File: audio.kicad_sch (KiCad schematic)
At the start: 6 parts, among them J6 AudioJack3, U8 LM386

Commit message: Updated Schematic
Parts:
- added C37: 250 uF, Capacitor_SMD:C_0805_2012Metric, symbol Device:C
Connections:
- net +5V: no longer C35.2
- net at C36.2, U8.5: now also C37.1; no longer J6.R, J6.T
- new net: C37.2, J6.R, J6.T
- new net AUDIO_IN: C35.2
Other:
- moved on the sheet: J6
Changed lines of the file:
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@@
 	(paper "A4")
 	(junction
-		(at 168.91 86.36)
+		(at 184.15 86.36)
 		(diameter 0)
 		(color 0 0 0 0)
@@
 	(wire
 		(pts
-			(xy 168.91 83.82) (xy 168.91 86.36)
+			(xy 184.15 83.82) (xy 184.15 86.36)
 		)
 		(stroke
@@
 	(wire
 		(pts
+			(xy 176.53 86.36) (xy 184.15 86.36)
+		)
+		(stroke
+			(width 0)
+			(type default)
+		)
+	)
+	(wire
+		(pts
 			(xy 135.89 88.9) (xy 130.81 88.9)
 		)
@@
 	(wire
 		(pts
-			(xy 171.45 88.9) (xy 171.45 93.98)
-		)
-		(stroke
-			(width 0)
-			(type default)
-		)
-	)
-	(wire
-		(pts
-			(xy 171.45 83.82) (xy 168.91 83.82)
+			(xy 186.69 88.9) (xy 186.69 93.98)
+		)
+		(stroke
+			(width 0)
+			(type default)
+		)
+	)
+	(wire
+		(pts
+			(xy 186.69 83.82) (xy 184.15 83.82)
+		)
+		(stroke
+			(width 0)
+			(type default)
+		)
+	)
+	(wire
+		(pts
+			(xy 199.39 123.19) (xy 231.14 123.19)
 		)
 		(stroke
@@
 	(wire
 		(pts
-			(xy 168.91 86.36) (xy 171.45 86.36)
+			(xy 184.15 86.36) (xy 186.69 86.36)
 		)
 		(stroke
@@
 		)
 	)
-	(symbol
-		(lib_id "power:+5V")
-		(at 123.19 64.77 0)
-		(unit 1)
-		(exclude_from_sim no)
-		(in_bom yes)
-		(on_board yes)
-		(dnp no)
-		(fields_autoplaced yes)
-		(property "Reference" "#PWR072"
-			(at 123.19 68.58 0)
-			(effects
-				(font
-					(size 1.27 1.27)
-				)
-				(hide yes)
-			)
-		)
-		(property "Value" "+5V"
-			(at 123.19 59.69 0)
-			(effects
-				(font
-					(size 1.27 1.27)
-				)
-			)
-		)
-		(property "Footprint" ""
-			(at 123.19 64.77 0)
-			(effects
-				(font
-					(size 1.27 1.27)
-				)
-				(hide yes)
-			)
-		)
-		(property "Datasheet" ""
-			(at 123.19 64.77 0)
-			(effects
-				(font
-					(size 1.27 1.27)
-				)
-				(hide yes)
-			)
-		)
-		(property "Description" "Power symbol creates a global label with name \"+5V\""
-			(at 123.19 64.77 0)
-			(effects
-				(font
-					(size 1.27 1.27)
-				)
-				(hide yes)
-			)
-		)
-		(pin "1"
-		)
-		(instances
-			(project ""
-				(path "/35c074f0-8545-4dc1-a57d-3ef0bc7d9188/b0fb54ab-b2e8-4f49-90f2-51362383cff9"
-					(reference "#PWR072")
-					(unit 1)
-				)
-			)
+	(global_label "AUDIO_OUT"
+		(shape input)
+		(at 199.39 123.19 180)
+		(fields_autoplaced yes)
+		(effects
+			(font
+				(size 1.27 1.27)
+			)
+			(justify right)
+		)
+		(property "Intersheetrefs" "${INTERSHEET_REFS}"
+			(at 186.1842 123.19 0)
+			(effects
+				(font
+					(size 1.27 1.27)
+				)
+				(justify right)
+				(hide yes)
+			)
+		)
+	)
+	(global_label "AUDIO_IN"
+		(shape input)
+		(at 123.19 64.77 90)
+		(fields_autoplaced yes)
+		(effects
+			(font
+				(size 1.27 1.27)
+			)
+			(justify left)
+		)
+		(property "Intersheetrefs" "${INTERSHEET_REFS}"
+			(at 123.19 53.2575 90)
+			(effects
+				(font
+					(size 1.27 1.27)
+				)
+				(justify left)
+				(hide yes)
+			)
+		)
+	)
+	(hierarchical_label "AUDIO_IN"
+		(shape input)
+		(at 231.14 123.19 0)
+		(effects
+			(font
+				(size 1.27 1.27)
+			)
+			(justify left)
 		)
 	)
@@
 	(symbol
 		(lib_id "power:GND")
-		(at 171.45 93.98 0)
+		(at 186.69 93.98 0)
 		(unit 1)
 		(exclude_from_sim no)
@@
 		(fields_autoplaced yes)
 		(property "Reference" "#PWR071"
-			(at 171.45 100.33 0)
+			(at 186.69 100.33 0)
 			(effects
 				(font
@@
 		)
 		(property "Value" "GND"
-			(at 171.45 99.06 0)
+			(at 186.69 99.06 0)
 			(effects
 				(font
@@
 		)
 		(property "Footprint" ""
-			(at 171.45 93.98 0)
+			(at 186.69 93.98 0)
 			(effects
 				(font
@@
 		)
 		(property "Datasheet" ""
-			(at 171.45 93.98 0)
+			(at 186.69 93.98 0)
 			(effects
 				(font
@@
 		)
 		(property "Description" "Power symbol creates a global label with name \"GND\" , ground"
-			(at 171.45 93.98 0)
+			(at 186.69 93.98 0)
 			(effects
 				(font
@@
 	(symbol
 		(lib_id "Connector_Audio:AudioJack3")
-		(at 176.53 86.36 180)
+		(at 191.77 86.36 180)
 		(unit 1)
 		(exclude_from_sim no)
@@
 		(fields_autoplaced yes)
 		(property "Reference" "J6"
-			(at 184.15 84.4549 0)
+			(at 199.39 84.4549 0)
 			(effects
 				(font
@@
 		)
 		(property "Value" "AudioJack3"
-			(at 184.15 86.9949 0)
+			(at 199.39 86.9949 0)
 			(effects
 				(font
@@
 		)
 		(property "Footprint" "Connector_Audio:Jack_3.5mm_CUI_SJ-3523-SMT_Horizontal"
-			(at 176.53 86.36 0)
+			(at 191.77 86.36 0)
 			(effects
 				(font
@@
 		)
 		(property "Datasheet" "~"
-			(at 176.53 86.36 0)
+			(at 191.77 86.36 0)
 			(effects
 				(font
@@
 		)
 		(property "Description" "Audio Jack, 3 Poles (Stereo / TRS)"
-			(at 176.53 86.36 0)
+			(at 191.77 86.36 0)
 			(effects
 				(font
@@
 					(unit 1)
 				)
+			)
+		)
+	)
+	(symbol
+		(lib_id "Device:C")
+		(at 172.72 86.36 90)
+		(unit 1)
+		(exclude_from_sim no)
+		(in_bom yes)
+		(on_board yes)
+		(dnp no)
+		(fields_autoplaced yes)
+		(property "Reference" "C37"
+			(at 172.72 78.74 90)
+			(effects
+				(font
+					(size 1.27 1.27)
+				)
+			)
+		)
+		(property "Value" "250 uF"
+			(at 172.72 81.28 90)
+			(effects
+				(font
+					(size 1.27 1.27)
+				)
+			)
+		)
+		(property "Footprint" "Capacitor_SMD:C_0805_2012Metric"
+			(at 176.53 85.3948 0)
+			(effects
+				(font
+					(size 1.27 1.27)
+				)
+				(hide yes)
+			)
+		)
+		(property "Datasheet" "~"
+			(at 172.72 86.36 0)
+			(effects
+				(font
+					(size 1.27 1.27)
+				)
+				(hide yes)
+			)
+		)
+		(property "Description" "Unpolarized capacitor"
+			(at 172.72 86.36 0)
+			(effects
+				(font
+					(size 1.27 1.27)
+				)
+				(hide yes)
+			)
+		)
+		(pin "1"
+		)
+		(pin "2"
+		)
+		(instances
+			(project ""
+				(path "/35c074f0-8545-4dc1-a57d-3ef0bc7d9188/b0fb54ab-b2e8-4f49-90f2-51362383cff9"
+					(reference "C37")
+					(unit 1)
+				)

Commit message: Updated Schematic
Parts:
- added D8: D_TVS, symbol Device:D_TVS
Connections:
- net at C37.2, J6.R, J6.T: now also D8.2 (A2)
- net GND renamed GNDA
- net GNDA: now also D8.1 (A1)

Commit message: Updated Audio with ESD Diode
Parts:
- D8: footprint (none) -> Audio_Module:D_TVS SMB
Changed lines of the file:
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@@
 			)
 		)
-		(property "Footprint" ""
+		(property "Footprint" "Audio_Module:D_TVS SMB"
 			(at 177.8 90.17 0)
 			(effects

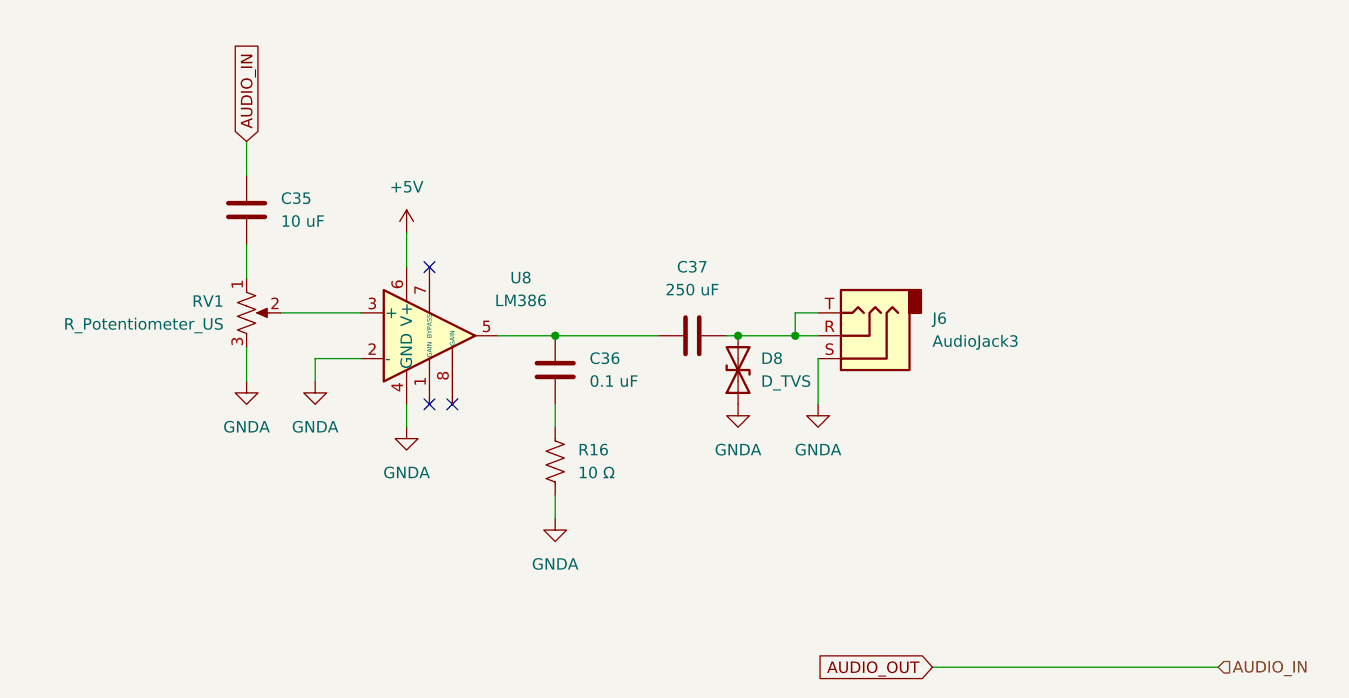
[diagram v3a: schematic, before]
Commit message: fixed a bunch of DRC errors
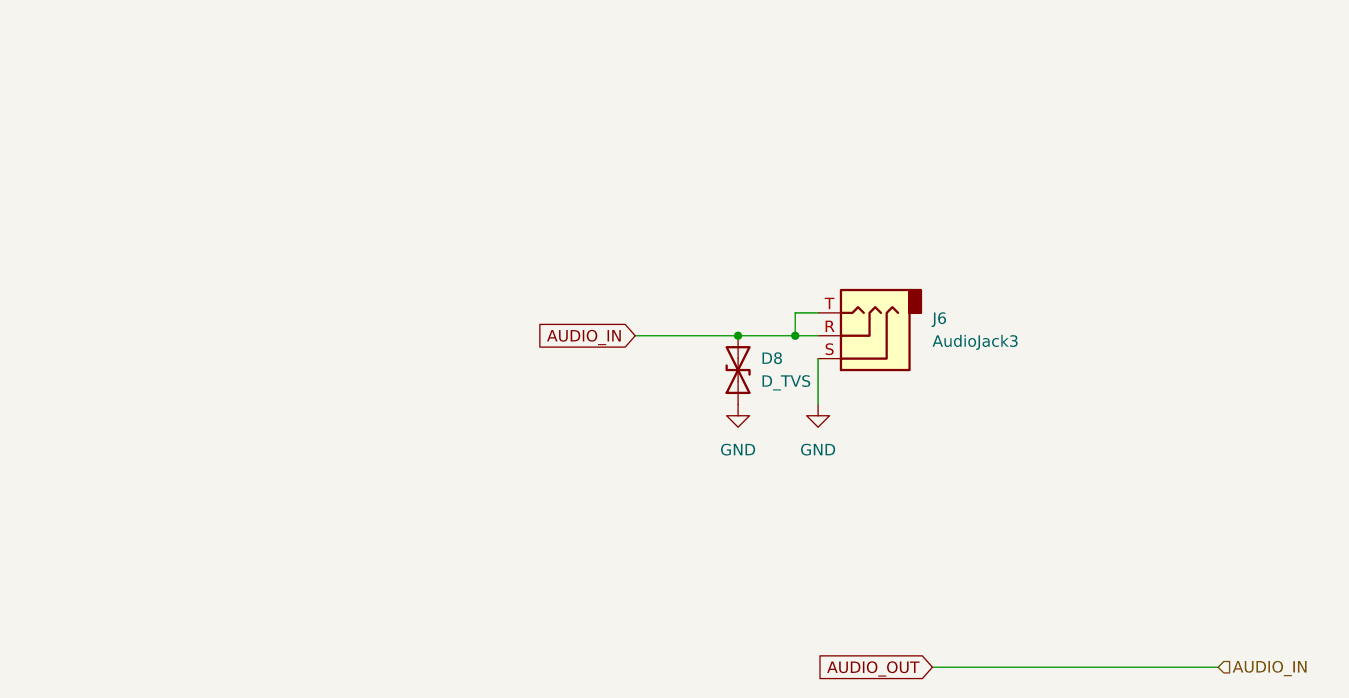
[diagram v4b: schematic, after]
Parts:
- removed C35: 10 uF, Capacitor_SMD:C_0805_2012Metric, symbol Device:C
- removed C36: 0.1 uF, Capacitor_SMD:C_0805_2012Metric, symbol Device:C
- removed C37: 250 uF, Capacitor_SMD:C_0805_2012Metric, symbol Device:C
- removed R16: 10 Ω, Resistor_SMD:R_0805_2012Metric, symbol Device:R_US
- removed RV1: R_Potentiometer_US, Potentiometer_SMD:Potentiometer_Bourns_3214G_Horizontal, symbol Device:R_Potentiometer_US
- removed U8: LM386, Library:LM386, symbol Amplifier_Audio:LM386
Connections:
- net AUDIO_IN: now also D8.2 (A2), J6.R, J6.T
- net GNDA renamed GND
- no-connect marks 3 -> 0

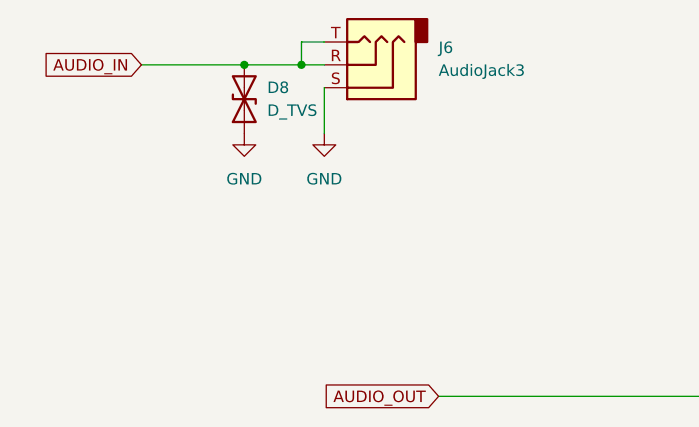
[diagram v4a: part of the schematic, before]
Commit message: Fixed labels and added datasheets
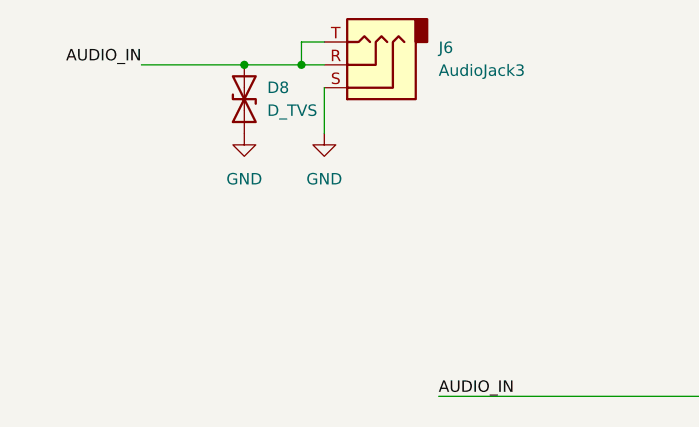
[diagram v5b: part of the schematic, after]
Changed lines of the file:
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@@
 		)
 	)
-	(global_label "AUDIO_OUT"
-		(shape input)
-		(at 199.39 123.19 180)
-		(fields_autoplaced yes)
+	(label "AUDIO_IN"
+		(at 166.37 86.36 180)
 		(effects
 			(font
 				(size 1.27 1.27)
 			)
-			(justify right)
-		)
-		(property "Intersheetrefs" "${INTERSHEET_REFS}"
-			(at 186.1842 123.19 0)
-			(effects
-				(font
-					(size 1.27 1.27)
-				)
-				(justify right)
-				(hide yes)
-			)
+			(justify right bottom)
 		)
 	)
-	(global_label "AUDIO_IN"
-		(shape input)
-		(at 166.37 86.36 180)
-		(fields_autoplaced yes)
+	(label "AUDIO_IN"
+		(at 199.39 123.19 0)
 		(effects
 			(font
 				(size 1.27 1.27)
 			)
-			(justify right)
-		)
-		(property "Intersheetrefs" "${INTERSHEET_REFS}"
-			(at 154.8575 86.36 0)
-			(effects
-				(font
-					(size 1.27 1.27)
-				)
-				(justify right)
-				(hide yes)
-			)
+			(justify left bottom)
 		)
 	)

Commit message: small changes
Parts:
- added C36: 6.8nF, Capacitor_SMD:C_0805_2012Metric_Pad1.18x1.45mm_HandSolder, symbol Device:C
- added C37: 10 uF, Capacitor_SMD:C_0805_2012Metric_Pad1.18x1.45mm_HandSolder, symbol Device:C
- added R51: 1k, Resistor_SMD:R_0805_2012Metric_Pad1.20x1.40mm_HandSolder, symbol Device:R
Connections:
- net AUDIO_IN: now also R51.1; no longer D8.2 (A2), J6.R, J6.T
- net GND: now also C36.2
- new net: C36.1, C37.1, R51.2
- new net: C37.2, D8.2 (A2), J6.R, J6.T

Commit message: fixed several issues from review
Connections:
- net GND renamed GNDA
